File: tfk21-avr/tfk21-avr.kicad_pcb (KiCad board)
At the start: 4 copper layers, 76.2 x 115.5 mm, 123 parts, among them J1 USB_C_Receptacle_USB2.0, J2 AVR-ISP-6, SW1 Reset, U1 ATmega32U4-AU, U2 IS31FL3733-TQ, Y1 16MHz

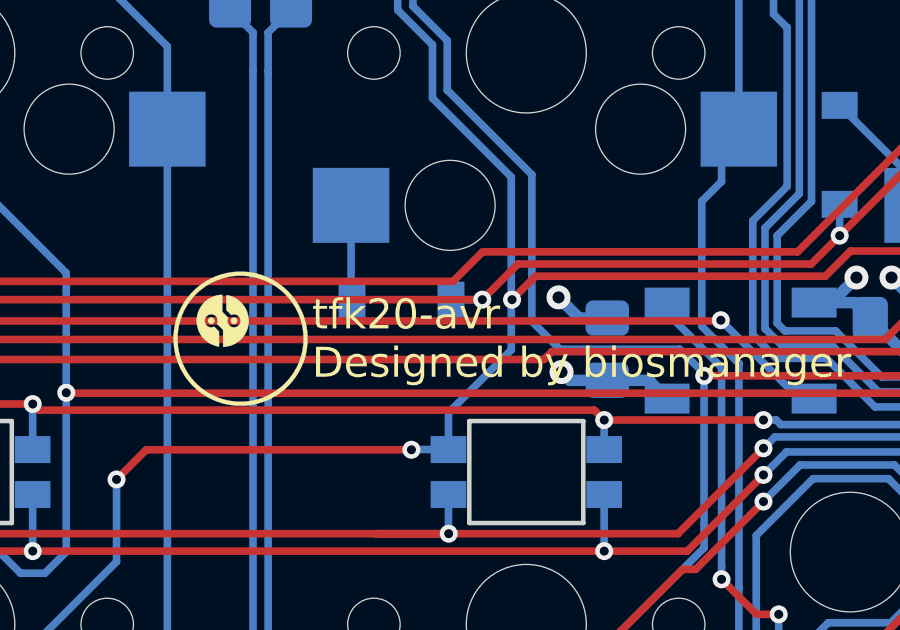
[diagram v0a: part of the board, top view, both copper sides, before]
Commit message: Rename tfk20 to tfk21
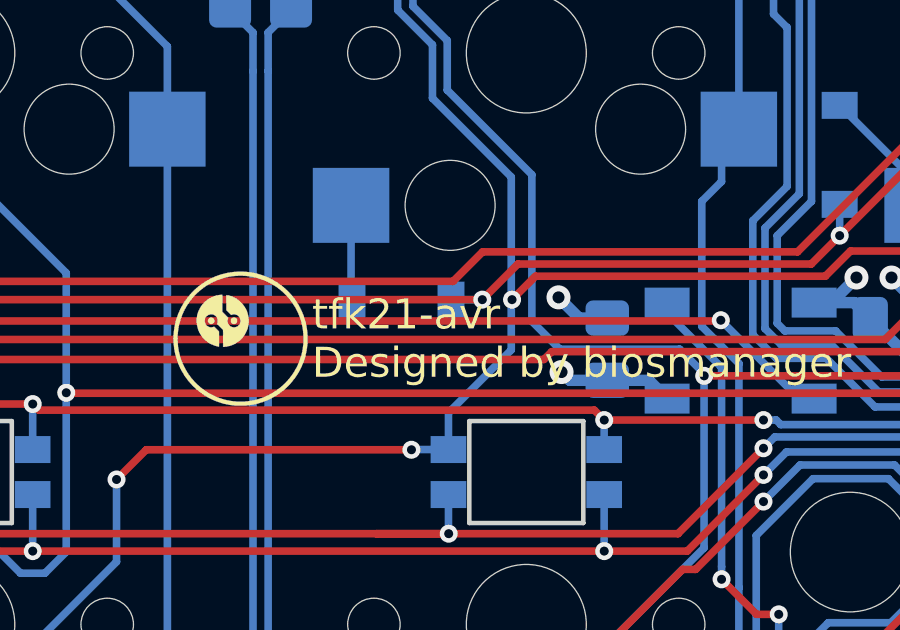
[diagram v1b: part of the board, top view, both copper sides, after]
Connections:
- net /tfk20 RGB Matrix/CS1 renamed /tfk21 RGB Matrix/CS1
- net /tfk20 RGB Matrix/CS2 renamed /tfk21 RGB Matrix/CS2
- net /tfk20 RGB Matrix/CS3 renamed /tfk21 RGB Matrix/CS3
- net /tfk20 RGB Matrix/CS4 renamed /tfk21 RGB Matrix/CS4
- net /tfk20 RGB Matrix/CS5 renamed /tfk21 RGB Matrix/CS5
- net /tfk20 RGB Matrix/CS6 renamed /tfk21 RGB Matrix/CS6
- net /tfk20 RGB Matrix/CS7 renamed /tfk21 RGB Matrix/CS7
- net /tfk20 RGB Matrix/CS8 renamed /tfk21 RGB Matrix/CS8
- net /tfk20 RGB Matrix/SW1 renamed /tfk21 RGB Matrix/SW1
- net /tfk20 RGB Matrix/SW2 renamed /tfk21 RGB Matrix/SW2
- net /tfk20 RGB Matrix/SW3 renamed /tfk21 RGB Matrix/SW3
- net /tfk20 RGB Matrix/SW4 renamed /tfk21 RGB Matrix/SW4
- net /tfk20 RGB Matrix/SW5 renamed /tfk21 RGB Matrix/SW5
- net /tfk20 RGB Matrix/SW6 renamed /tfk21 RGB Matrix/SW6
- net /tfk20 RGB Matrix/SW7 renamed /tfk21 RGB Matrix/SW7
- net /tfk20 RGB Matrix/SW8 renamed /tfk21 RGB Matrix/SW8
- net /tfk20 RGB Matrix/SW9 renamed /tfk21 RGB Matrix/SW9
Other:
- board text added: "tfk21 Rev. A"
- board text added: "tfk21-avr Designed by biosmanager"
- board text removed: "tfk20 Rev. A"
- board text removed: "tfk20-avr Designed by biosmanager"

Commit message: Add 3D models
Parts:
- H5, H6, H7: moved to F.Cu
- turned H5 to 270 degrees
- turned H6 to 270 degrees
- turned H7 to 180 degrees
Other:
- board text added: "Designed by biosmanager"
- board text added: "tfk21-avr"
- board text added: "tfk21-avr Rev. A"
- board text removed: "tfk21 Rev. A"
- board text removed: "tfk21-avr Designed by biosmanager"
